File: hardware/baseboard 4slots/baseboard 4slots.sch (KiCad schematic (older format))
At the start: 24 parts, among them J1 IO-Board_00, J2 IO-Board_01, J3 IO-Board_10, J4 IO-Board_11, J5 USB_B_Micro, J6 Conn_01x05: Adafruit 1833, J7 Screw_Terminal_01x04, J8 Conn_02x02_Odd_Even, J9 Conn_02x02_Odd_Even, U1 NRF24L01_Breakout, U2 Pico

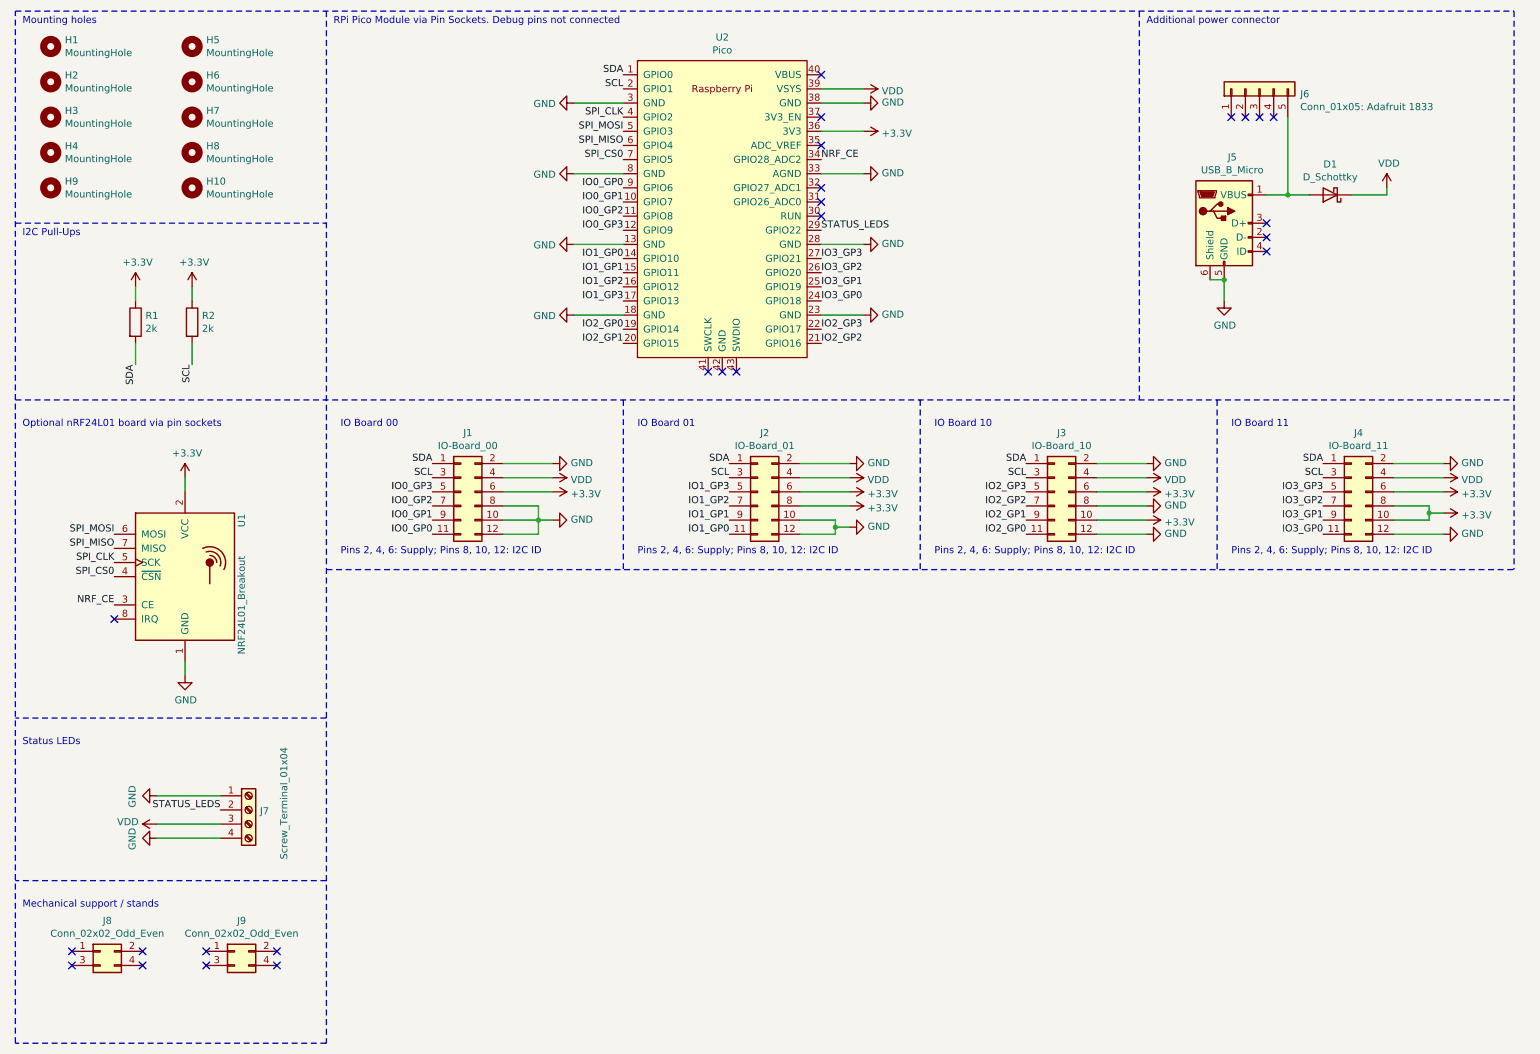
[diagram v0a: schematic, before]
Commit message: Baseboard: Add some capacitors between GND and supply lines (nRF24 connector, RPi Pico, status LEDs and IO connectors)
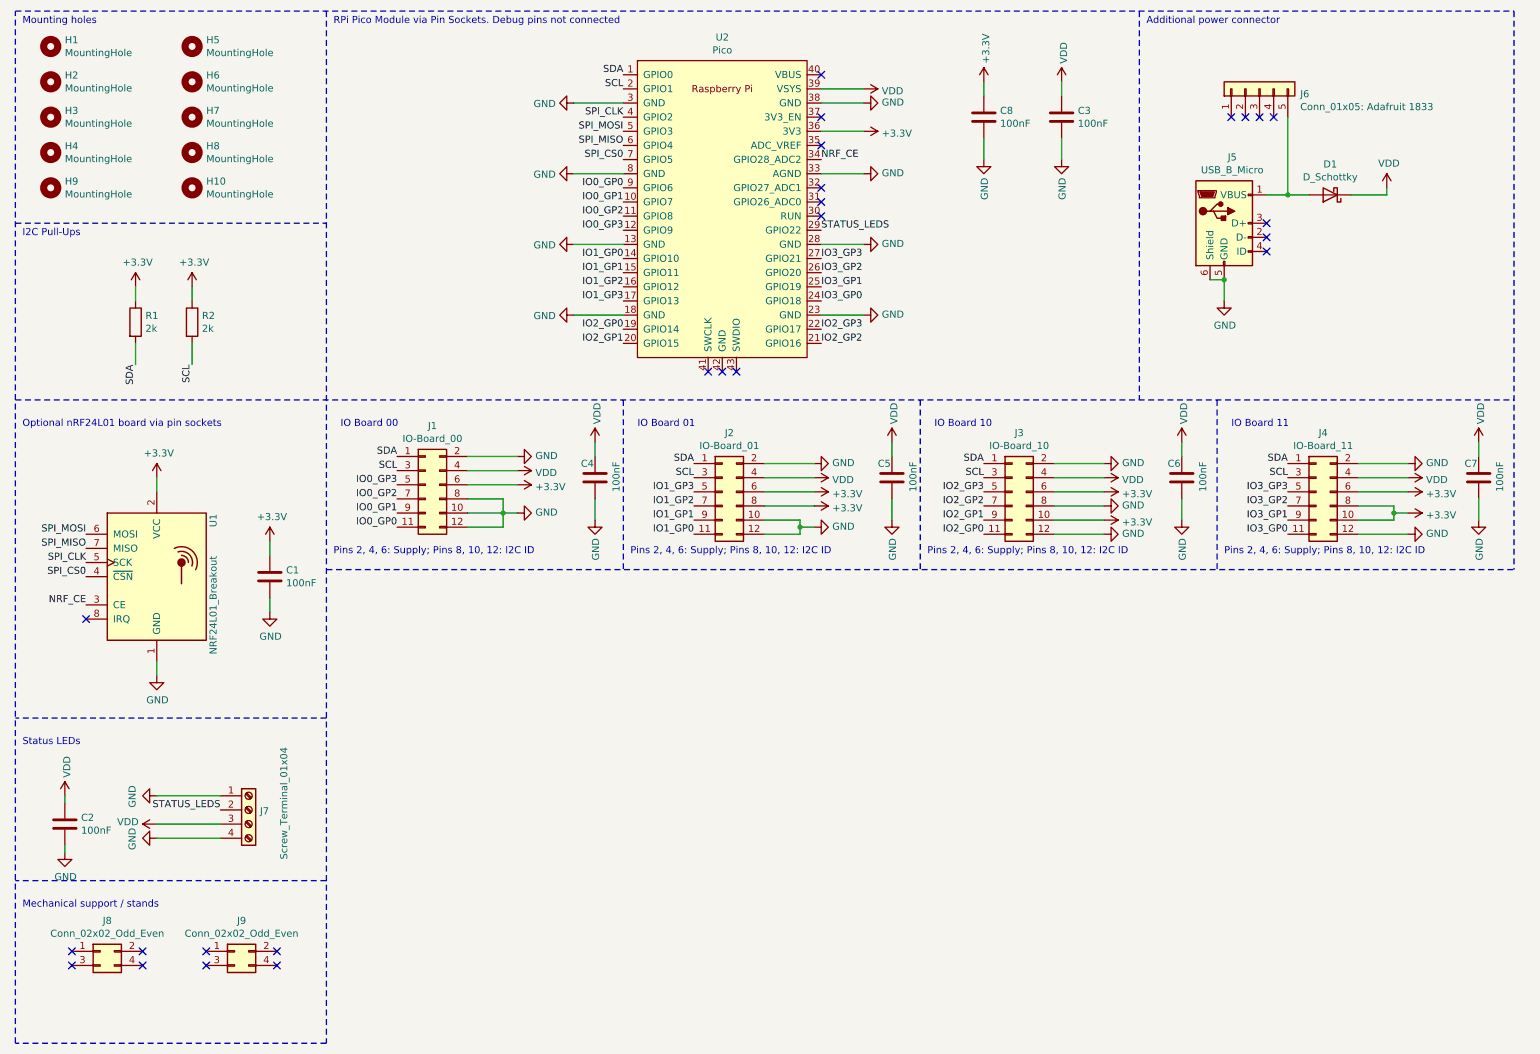
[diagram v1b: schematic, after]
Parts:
- added C1, C2, C3, C4, C5, C6, C7, C8: 100nF, Capacitor_SMD:C_0603_1608Metric, symbol Device:C
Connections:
- net +3V3: now also C1.1, C8.1
- net GND: now also C1.2, C2.2, C3.2, C4.2, C5.2, C6.2, C7.2, C8.2
- net VDD: now also C2.1, C3.1, C4.1, C5.1, C6.1, C7.1
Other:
- moved on the sheet: J1, J2, J3, J4, U1

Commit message: Hardware: Several fixes and improvements in schematics and PCBs (more capacitors, alternative footprint for DC/DC converter, more GND stitching, better trace placement, ...)
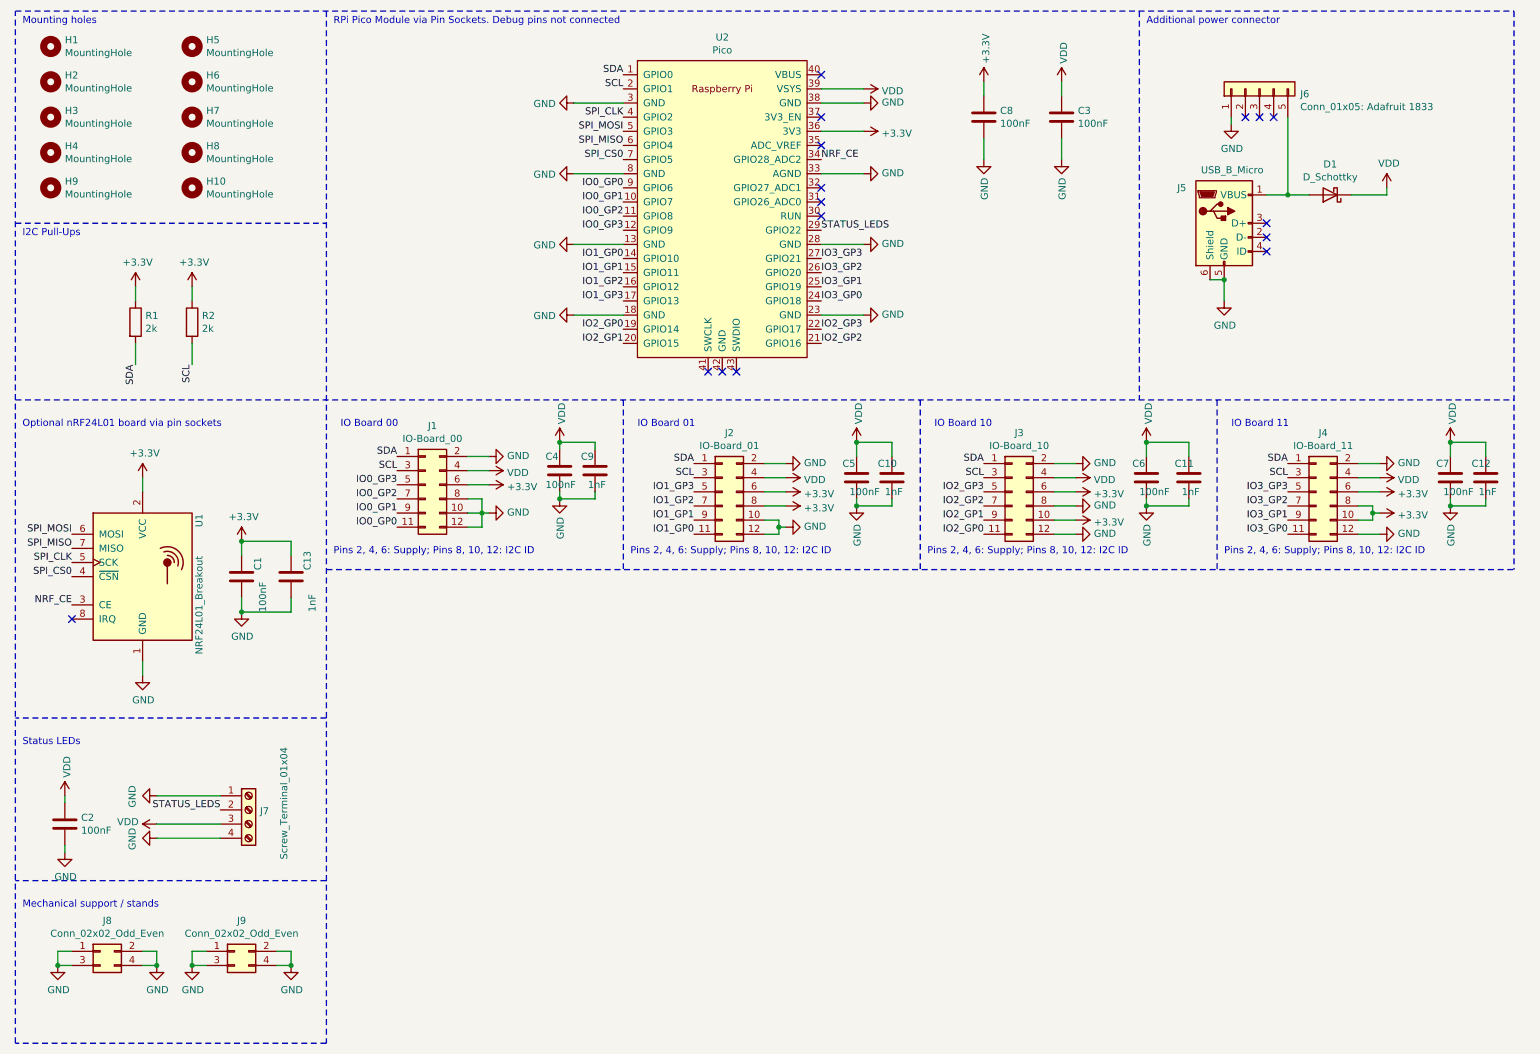
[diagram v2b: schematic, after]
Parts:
- added C10, C11, C12, C13, C9: 1nF, Capacitor_SMD:C_0603_1608Metric, symbol Device:C
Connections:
- net +3V3: now also C13.1
- net GND: now also J6.1 (Pin_1), J8.1 (Pin_1), J8.2 (Pin_2), J8.3 (Pin_3), J8.4 (Pin_4), J9.1 (Pin_1), J9.2 (Pin_2), J9.3 (Pin_3), J9.4 (Pin_4), C10.2, C11.2, C12.2, C13.2, C9.2
- net VDD: now also C10.1, C11.1, C12.1, C9.1
- no-connect marks 25 -> 16
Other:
- moved on the sheet: C1, C4, C5, C6, C7, U1

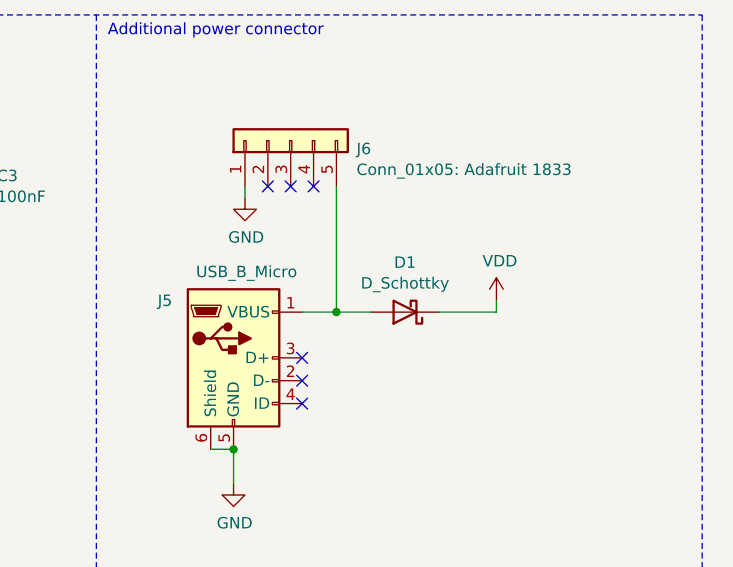
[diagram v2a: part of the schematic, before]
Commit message: Add LCSC part numbers to the schematic for production :)
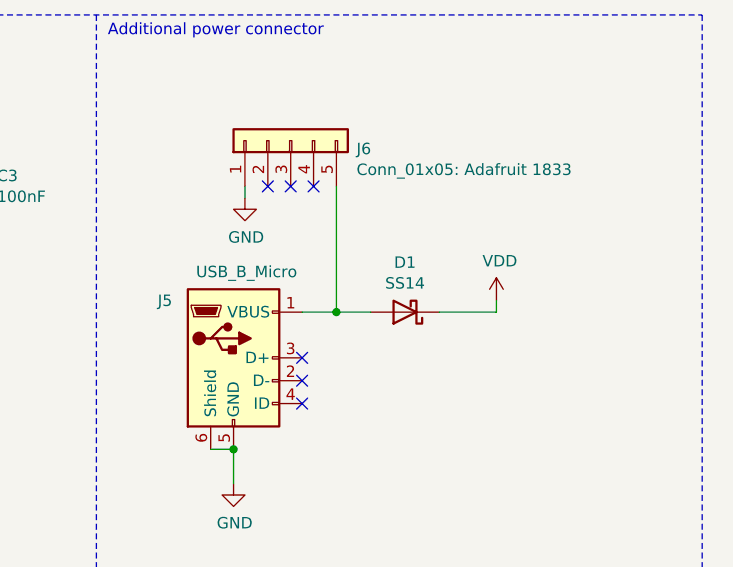
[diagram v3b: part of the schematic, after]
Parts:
- C1, C2, C3, C4, C5, C6, C7, C8: LCSC (none) -> C14663
- C10, C11, C12, C13: LCSC (none) -> C1588
- D1: value D_Schottky -> SS14; LCSC (none) -> C2480
- R1, R2: LCSC (none) -> C17604
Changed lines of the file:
@@
 F 2 "Resistor_SMD:R_0805_2012Metric_Pad1.20x1.40mm_HandSolder" V 1680 2700 50  0001 C CNN
 F 3 "~" H 1750 2700 50  0001 C CNN
+F 4 "C17604" H 1750 2700 50  0001 C CNN "LCSC"
 	1    1750 2700
 	1    0    0    -1
@@
 F 2 "Resistor_SMD:R_0805_2012Metric_Pad1.20x1.40mm_HandSolder" V 1280 2700 50  0001 C CNN
 F 3 "~" H 1350 2700 50  0001 C CNN
+F 4 "C17604" H 1350 2700 50  0001 C CNN "LCSC"
 	1    1350 2700
 	1    0    0    -1
@@
 P 9800 1800
 F 0 "D1" H 9800 1583 50  0000 C CNN
-F 1 "D_Schottky" H 9800 1674 50  0000 C CNN
+F 1 "SS14" H 9800 1674 50  0000 C CNN
 F 2 "Diode_SMD:D_SMA" H 9800 1800 50  0001 C CNN
 F 3 "~" H 9800 1800 50  0001 C CNN
+F 4 "C2480" H 9800 1800 50  0001 C CNN "LCSC"
 	1    9800 1800
 	-1   0    0    1
@@
 F 2 "Capacitor_SMD:C_0603_1608Metric" H 2138 4350 50  0001 C CNN
 F 3 "~" H 2100 4500 50  0001 C CNN
+F 4 "C14663" V 2100 4500 50  0001 C CNN "LCSC"
 	1    2100 4500
 	1    0    0    -1
@@
 F 2 "Capacitor_SMD:C_0603_1608Metric" H 888 6100 50  0001 C CNN
 F 3 "~" H 850 6250 50  0001 C CNN
+F 4 "C14663" H 850 6250 50  0001 C CNN "LCSC"
 	1    850  6250
 	1    0    0    -1
@@
 F 2 "Capacitor_SMD:C_0603_1608Metric" H 7938 1100 50  0001 C CNN
 F 3 "~" H 7900 1250 50  0001 C CNN
+F 4 "C14663" H 7900 1250 50  0001 C CNN "LCSC"
 	1    7900 1250
 	1    0    0    -1
@@
 F 2 "Capacitor_SMD:C_0603_1608Metric" H 4388 3600 50  0001 C CNN
 F 3 "~" H 4350 3750 50  0001 C CNN
+F 4 "C14663" H 4350 3750 50  0001 C CNN "LCSC"
 	1    4350 3750
 	1    0    0    -1
@@
 F 2 "Capacitor_SMD:C_0603_1608Metric" H 6488 3650 50  0001 C CNN
 F 3 "~" H 6450 3800 50  0001 C CNN
+F 4 "C14663" H 6450 3800 50  0001 C CNN "LCSC"
 	1    6450 3800
 	1    0    0    -1
@@
 F 2 "Capacitor_SMD:C_0603_1608Metric" H 8538 3650 50  0001 C CNN
 F 3 "~" H 8500 3800 50  0001 C CNN
+F 4 "C14663" H 8500 3800 50  0001 C CNN "LCSC"
 	1    8500 3800
 	1    0    0    -1
@@
 F 2 "Capacitor_SMD:C_0603_1608Metric" H 10688 3650 50  0001 C CNN
 F 3 "~" H 10650 3800 50  0001 C CNN
+F 4 "C14663" H 10650 3800 50  0001 C CNN "LCSC"
 	1    10650 3800
 	1    0    0    -1
@@
 F 2 "Capacitor_SMD:C_0603_1608Metric" H 7388 1100 50  0001 C CNN
 F 3 "~" H 7350 1250 50  0001 C CNN
+F 4 "C14663" H 7350 1250 50  0001 C CNN "LCSC"
 	1    7350 1250
 	1    0    0    -1
@@
 F 2 "Capacitor_SMD:C_0603_1608Metric" H 2488 4350 50  0001 C CNN
 F 3 "~" H 2450 4500 50  0001 C CNN
+F 4 "C1588" V 2450 4500 50  0001 C CNN "LCSC"
 	1    2450 4500
 	1    0    0    -1
@@
 F 2 "Capacitor_SMD:C_0603_1608Metric" H 6738 3650 50  0001 C CNN
 F 3 "~" H 6700 3800 50  0001 C CNN
+F 4 "C1588" H 6700 3800 50  0001 C CNN "LCSC"
 	1    6700 3800
 	1    0    0    -1
@@
 F 2 "Capacitor_SMD:C_0603_1608Metric" H 8838 3650 50  0001 C CNN
 F 3 "~" H 8800 3800 50  0001 C CNN
+F 4 "C1588" H 8800 3800 50  0001 C CNN "LCSC"
 	1    8800 3800
 	1    0    0    -1
@@
 F 2 "Capacitor_SMD:C_0603_1608Metric" H 10938 3650 50  0001 C CNN
 F 3 "~" H 10900 3800 50  0001 C CNN
+F 4 "C1588" H 10900 3800 50  0001 C CNN "LCSC"
 	1    10900 3800
 	1    0    0    -1
